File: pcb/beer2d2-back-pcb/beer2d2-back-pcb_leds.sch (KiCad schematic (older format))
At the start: 195 parts, among them Q1 DDTD113ZC, Q10 DDTB113ZC, Q11 DDTB113ZC, Q12 DDTB113ZC, Q13 DDTB113ZC, Q14 DDTB113ZC, Q15 DDTB113ZC, Q16 DDTB113ZC, Q17 DDTB113ZC, Q18 DDTB113ZC, Q19 DDTB113ZC, Q2 DDTD113ZC, Q3 DDTD113ZC, Q4 DDTD113ZC, Q5 DDTD113ZC, Q6 DDTD113ZC, Q7 DDTD113ZC, Q8 DDTD113ZC, Q9 DDTB113ZC

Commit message: tentative placement layout
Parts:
- removed R10, R12, R14, R16, R18, R20, R22, R24, R26, R28, R29, R30, R31, R32, R33, R34, R35, R36, R37, R38, R39, R40, R41, R42, R43, R44, R45, R46, R47, R48, R49, R50, R51, R52, R53, R54, R55, R56, R57, R58, R59, R60, R61, R62, R63, R64, R65, R66, R67, R68, R69, R70, R71, R72, R73, R74, R75, R76, R77, R78, R79, R8, R80, R81, R82, R83, R84, R85, R86, R87, R88, R89, R90, R91, R92, R93, R94: 110Ω, symbol R
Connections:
- net COL0: now also R7.1; no longer LED10.2 (A), LED3.2 (A), LED4.2 (A), LED5.2 (A), LED6.2 (A), LED7.2 (A), LED8.2 (A), LED9.2 (A)
- net COL1: now also R9.1; no longer LED11.2 (A), LED12.2 (A), LED13.2 (A), LED14.2 (A), LED15.2 (A), LED16.2 (A), LED17.2 (A), LED18.2 (A)
- net COL10: now also R27.1; no longer LED83.2 (A), LED84.2 (A), LED85.2 (A), LED86.2 (A), LED87.2 (A), LED88.2 (A), LED89.2 (A), LED90.2 (A)
- net COL2: now also R11.1; no longer LED19.2 (A), LED20.2 (A), LED21.2 (A), LED22.2 (A), LED23.2 (A), LED24.2 (A), LED25.2 (A), LED26.2 (A)
- net COL3: now also R13.1; no longer LED27.2 (A), LED28.2 (A), LED29.2 (A), LED30.2 (A), LED31.2 (A), LED32.2 (A), LED33.2 (A), LED34.2 (A)
- net COL4: now also R15.1; no longer LED35.2 (A), LED36.2 (A), LED37.2 (A), LED38.2 (A), LED39.2 (A), LED40.2 (A), LED41.2 (A), LED42.2 (A)
- net COL5: now also R17.1; no longer LED43.2 (A), LED44.2 (A), LED45.2 (A), LED46.2 (A), LED47.2 (A), LED48.2 (A), LED49.2 (A), LED50.2 (A)
- net COL6: now also R19.1; no longer LED51.2 (A), LED52.2 (A), LED53.2 (A), LED54.2 (A), LED55.2 (A), LED56.2 (A), LED57.2 (A), LED58.2 (A)
- net COL7: now also R21.1; no longer LED59.2 (A), LED60.2 (A), LED61.2 (A), LED62.2 (A), LED63.2 (A), LED64.2 (A), LED65.2 (A), LED66.2 (A)
- net COL8: now also R23.1; no longer LED67.2 (A), LED68.2 (A), LED69.2 (A), LED70.2 (A), LED71.2 (A), LED72.2 (A), LED73.2 (A), LED74.2 (A)
- net COL9: now also R25.1; no longer LED75.2 (A), LED76.2 (A), LED77.2 (A), LED78.2 (A), LED79.2 (A), LED80.2 (A), LED81.2 (A), LED82.2 (A)
- net ROW0: now also LED11.1 (C), LED19.1 (C), LED27.1 (C), LED3.1 (C), LED35.1 (C), LED43.1 (C), LED51.1 (C), LED59.1 (C), LED67.1 (C), LED75.1 (C), LED83.1 (C); no longer R15.1, R23.1, R7.1
- net ROW1: now also LED12.1 (C), LED20.1 (C), LED28.1 (C), LED36.1 (C), LED4.1 (C), LED44.1 (C), LED52.1 (C), LED60.1 (C), LED68.1 (C), LED76.1 (C), LED84.1 (C)
- net ROW2: now also LED13.1 (C), LED21.1 (C), LED29.1 (C), LED37.1 (C), LED45.1 (C), LED5.1 (C), LED53.1 (C), LED61.1 (C), LED69.1 (C), LED77.1 (C), LED85.1 (C); no longer R17.1, R25.1, R9.1
- net ROW3: now also LED14.1 (C), LED22.1 (C), LED30.1 (C), LED38.1 (C), LED46.1 (C), LED54.1 (C), LED6.1 (C), LED62.1 (C), LED70.1 (C), LED78.1 (C), LED86.1 (C)
- net ROW4: now also LED15.1 (C), LED23.1 (C), LED31.1 (C), LED39.1 (C), LED47.1 (C), LED55.1 (C), LED63.1 (C), LED7.1 (C), LED71.1 (C), LED79.1 (C), LED87.1 (C); no longer R11.1, R19.1, R27.1
- net ROW5: now also LED16.1 (C), LED24.1 (C), LED32.1 (C), LED40.1 (C), LED48.1 (C), LED56.1 (C), LED64.1 (C), LED72.1 (C), LED8.1 (C), LED80.1 (C), LED88.1 (C)
- net ROW6: now also LED17.1 (C), LED25.1 (C), LED33.1 (C), LED41.1 (C), LED49.1 (C), LED57.1 (C), LED65.1 (C), LED73.1 (C), LED81.1 (C), LED89.1 (C), LED9.1 (C); no longer R13.1, R21.1
- net ROW7: now also LED10.1 (C), LED18.1 (C), LED26.1 (C), LED34.1 (C), LED42.1 (C), LED50.1 (C), LED58.1 (C), LED66.1 (C), LED74.1 (C), LED82.1 (C), LED90.1 (C)
- net at R15.2: now also LED35.2 (A), LED36.2 (A), LED37.2 (A), LED38.2 (A), LED39.2 (A), LED40.2 (A), LED41.2 (A), LED42.2 (A); no longer LED11.1 (C)
- net at R17.2: now also LED43.2 (A), LED44.2 (A), LED45.2 (A), LED46.2 (A), LED47.2 (A), LED48.2 (A), LED49.2 (A), LED50.2 (A); no longer LED13.1 (C)
- net at R23.2: now also LED67.2 (A), LED68.2 (A), LED69.2 (A), LED70.2 (A), LED71.2 (A), LED72.2 (A), LED73.2 (A), LED74.2 (A); no longer LED19.1 (C)
- net at R25.2: now also LED75.2 (A), LED76.2 (A), LED77.2 (A), LED78.2 (A), LED79.2 (A), LED80.2 (A), LED81.2 (A), LED82.2 (A); no longer LED21.1 (C)
- net at R19.2: now also LED51.2 (A), LED52.2 (A), LED53.2 (A), LED54.2 (A), LED55.2 (A), LED56.2 (A), LED57.2 (A), LED58.2 (A); no longer LED15.1 (C)
- net at R21.2: now also LED59.2 (A), LED60.2 (A), LED61.2 (A), LED62.2 (A), LED63.2 (A), LED64.2 (A), LED65.2 (A), LED66.2 (A); no longer LED17.1 (C)
- net at R27.2: now also LED83.2 (A), LED84.2 (A), LED85.2 (A), LED86.2 (A), LED87.2 (A), LED88.2 (A), LED89.2 (A), LED90.2 (A); no longer LED23.1 (C)
- net at R7.2: now also LED10.2 (A), LED3.2 (A), LED4.2 (A), LED5.2 (A), LED6.2 (A), LED7.2 (A), LED8.2 (A), LED9.2 (A); no longer LED3.1 (C)
- net at R9.2: now also LED11.2 (A), LED12.2 (A), LED13.2 (A), LED14.2 (A), LED15.2 (A), LED16.2 (A), LED17.2 (A), LED18.2 (A); no longer LED5.1 (C)
- net at R11.2: now also LED19.2 (A), LED20.2 (A), LED21.2 (A), LED22.2 (A), LED23.2 (A), LED24.2 (A), LED25.2 (A), LED26.2 (A); no longer LED7.1 (C)
- net at R13.2: now also LED27.2 (A), LED28.2 (A), LED29.2 (A), LED30.2 (A), LED31.2 (A), LED32.2 (A), LED33.2 (A), LED34.2 (A); no longer LED9.1 (C)
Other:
- note added: "LED Matrix"
- note added: "Left Half"
- note added: "Right Half"
- note removed: "Left Half LED Matrix"
- moved on the sheet: LED3, LED4, LED5, LED6

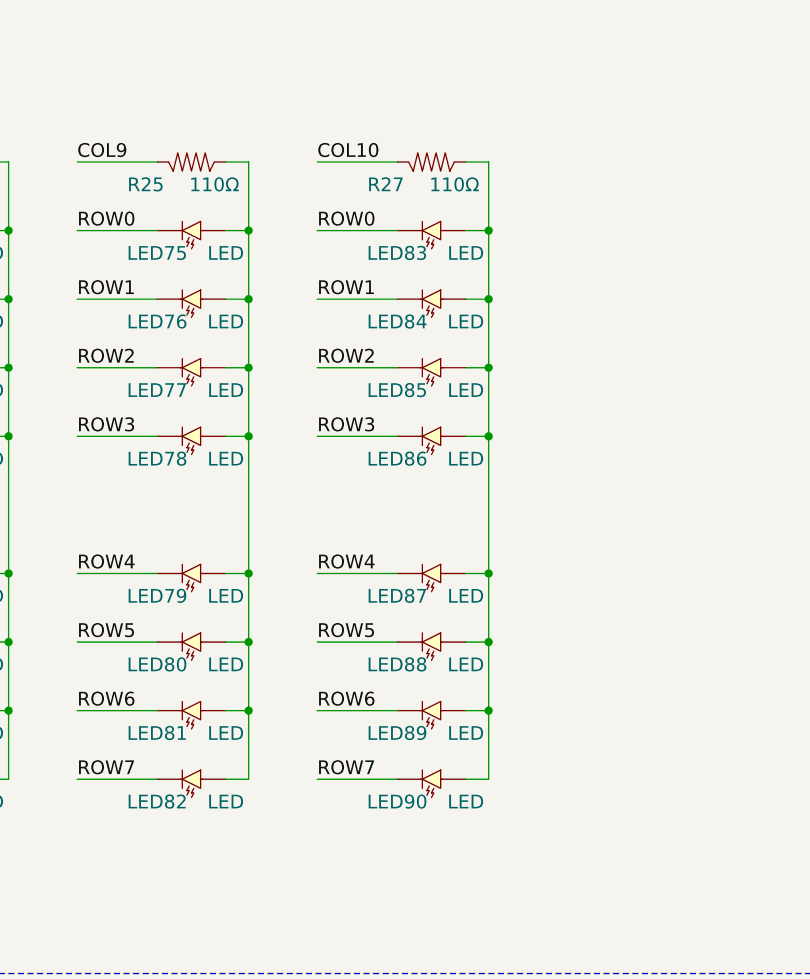
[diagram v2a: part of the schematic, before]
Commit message: continue routing for back pcb
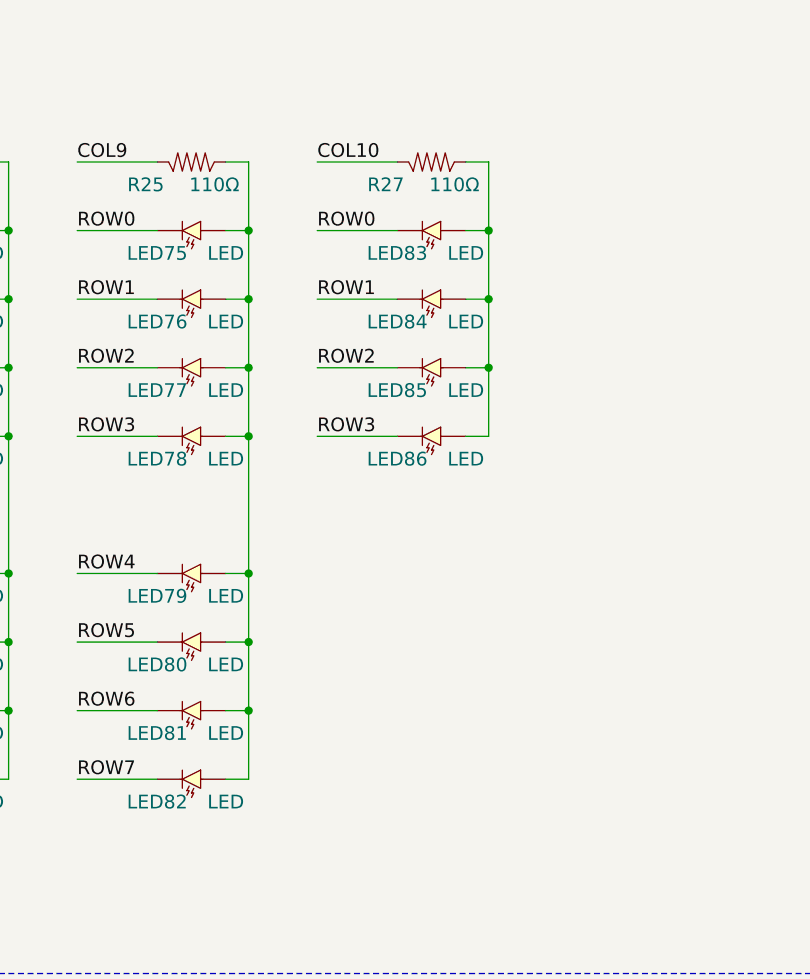
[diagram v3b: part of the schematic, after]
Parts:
- removed LED87, LED88, LED89, LED90: LED, symbol LED
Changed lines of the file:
@@
 LIBS:uln-ic
 LIBS:beer2d2-back-pcb-cache
-EELAYER 27 0
+EELAYER 24 0
 EELAYER END
 $Descr B 17000 11000
@@
 	12650 2100 12750 2100
 Wire Wire Line
-	12750 2100 12750 4800
-Wire Wire Line
 	12350 2100 12000 2100
 $Comp
@@
 Wire Wire Line
 	10950 3900 11300 3900
-$Comp
-L LED LED88
-U 1 1 52E6E73C
-P 12500 4200
-F 0 "LED88" H 12650 4300 60  0000 C CNN
-F 1 "LED" H 12350 4300 60  0000 C CNN
-F 2 "" H 12500 4200 60  0001 C CNN
-F 3 "" H 12500 4200 60  0001 C CNN
-	1    12500 4200
-	-1   0    0    1
-$EndComp
-$Comp
-L LED LED89
-U 1 1 52E6E742
-P 12500 4500
-F 0 "LED89" H 12650 4600 60  0000 C CNN
-F 1 "LED" H 12350 4600 60  0000 C CNN
-F 2 "" H 12500 4500 60  0001 C CNN
-F 3 "" H 12500 4500 60  0001 C CNN
-	1    12500 4500
-	-1   0    0    1
-$EndComp
-$Comp
-L LED LED90
-U 1 1 52E6E748
-P 12500 4800
-F 0 "LED90" H 12650 4900 60  0000 C CNN
-F 1 "LED" H 12350 4900 60  0000 C CNN
-F 2 "" H 12500 4800 60  0001 C CNN
-F 3 "" H 12500 4800 60  0001 C CNN
-	1    12500 4800
-	-1   0    0    1
-$EndComp
-Text Label 12000 3900 0    60   ~ 0
-ROW4
-Text Label 12000 4200 0    60   ~ 0
-ROW5
-Text Label 12000 4500 0    60   ~ 0
-ROW6
-Text Label 12000 4800 0    60   ~ 0
-ROW7
-Connection ~ 12750 4200
-Connection ~ 12750 4500
-Connection ~ 12750 3900
-Wire Wire Line
-	12650 4200 12750 4200
-Wire Wire Line
-	12650 4500 12750 4500
-Wire Wire Line
-	12750 4800 12650 4800
-Wire Wire Line
-	12000 4800 12350 4800
-$Comp
-L LED LED87
-U 1 1 52E6E75F
-P 12500 3900
-F 0 "LED87" H 12650 4000 60  0000 C CNN
-F 1 "LED" H 12350 4000 60  0000 C CNN
-F 2 "" H 12500 3900 60  0001 C CNN
-F 3 "" H 12500 3900 60  0001 C CNN
-	1    12500 3900
-	-1   0    0    1
-$EndComp
-Wire Wire Line
-	12000 4200 12350 4200
-Wire Wire Line
-	12000 4500 12350 4500
-Wire Wire Line
-	12650 3900 12750 3900
-Wire Wire Line
-	12000 3900 12350 3900
-Connection ~ 12750 3300
 Connection ~ 11700 3300
 Connection ~ 10650 3300
@@
 Text Notes 1250 1500 0    100  ~ 0
 Left Half
+Wire Wire Line
+	12750 2100 12750 3300
 $EndSCHEMATC
